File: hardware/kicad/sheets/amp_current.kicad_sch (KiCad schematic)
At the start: 22 parts, among them J11 AMP OUT (+ / -), J12 CRYOCOOLER (+ / -), U17 ISO7741DW, U18 ACS37800KMACTR-030B3-SPI

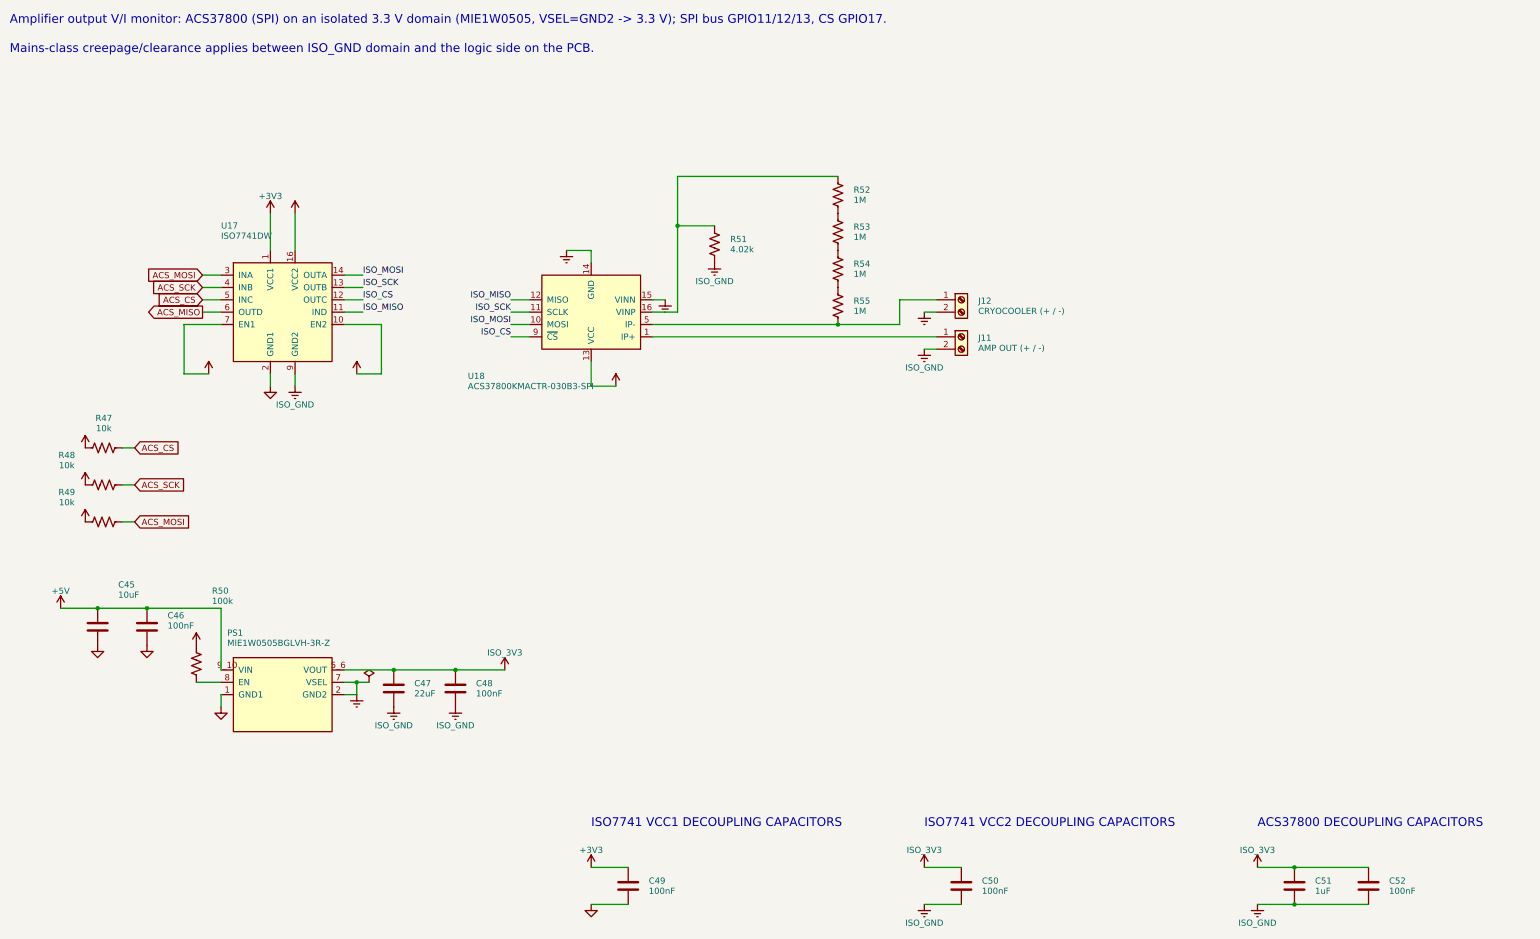
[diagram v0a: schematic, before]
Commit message: Put supply pins on top and grounds on the bottom of IC symbols; flake8-clean Python
Schematic: re-laid out pins on U2, U3, U6, U7, U11, U14, U17-U20, U22-U24
and PS1 (supply on top, ground/strap pins on the bottom edge) via custom
`cryocooler:` symbols (make_lib.from_stock) and a gnd_bus helper; U18/U2
use mirroring instead of a 180 degree rotation. Nets are unchanged (ERC 0,
117/117 datasheet rules, PCB nets still match). Text placement now shows
every power-symbol name, avoids wires, and uses a realistic character width.

Python: black -l 79 -S plus manual wrapping so hardware/kicad and scripts/
pass flake8; add .flake8.

Co-Authored-By: Claude Sonnet 5.5 <noreply@anthropic.com>
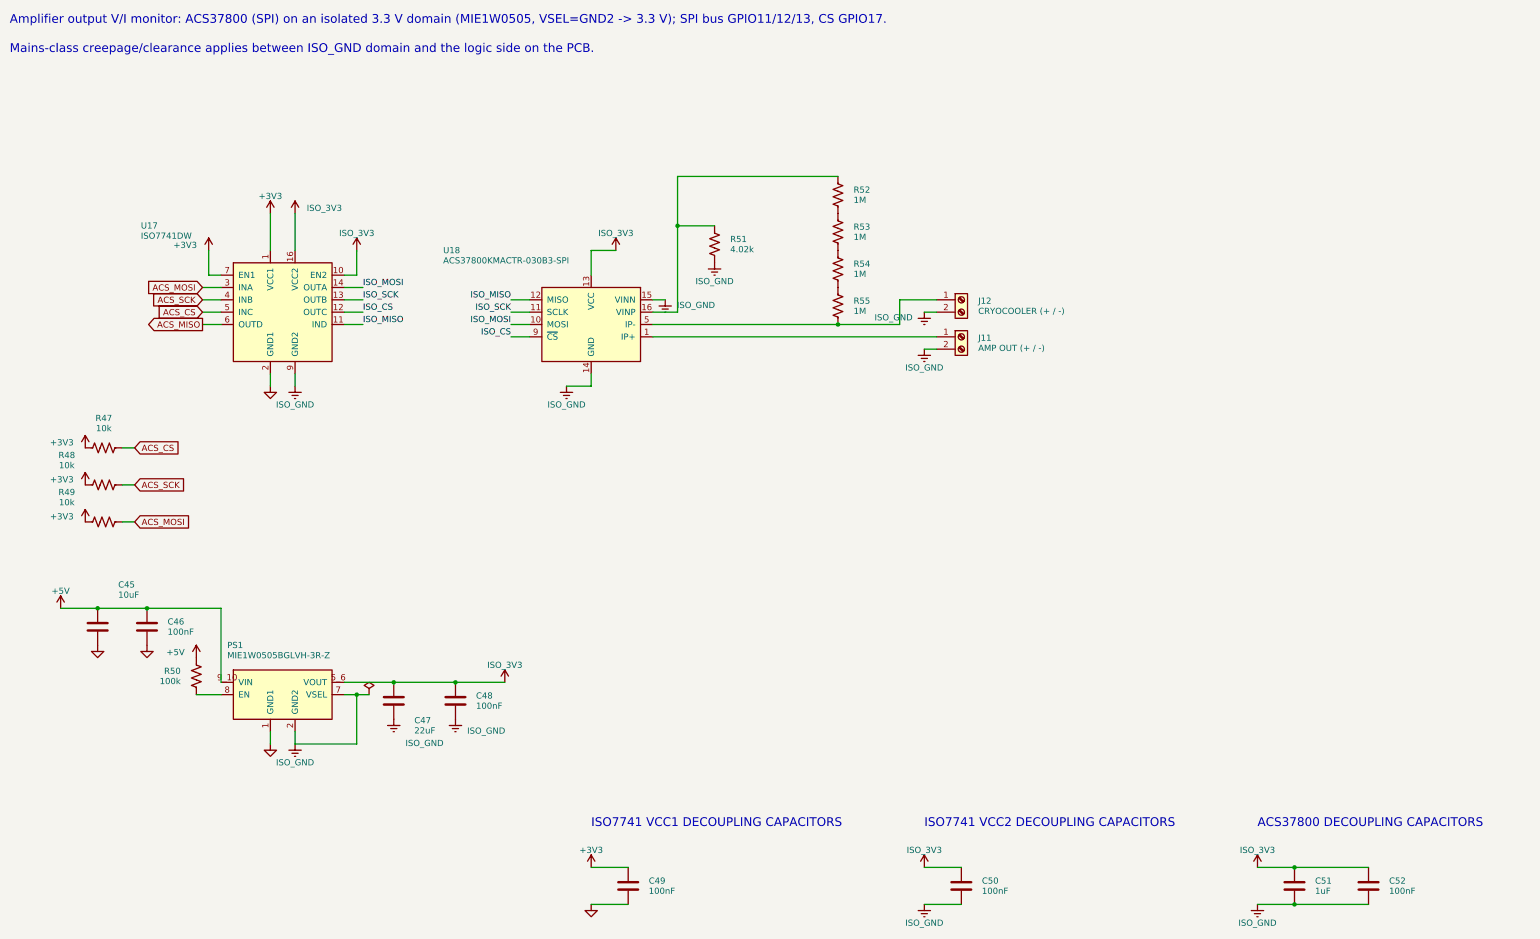
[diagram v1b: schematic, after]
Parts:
- removed C45: 10uF, Capacitor_SMD:C_0805_2012Metric, symbol Device:C
- removed C51: 1uF, Capacitor_SMD:C_0805_2012Metric, symbol Device:C
- removed J11: AMP OUT (+ / -), TerminalBlock_Phoenix:TerminalBlock_Phoenix_MKDS-1,5-2-5.08_1x02_P5.08mm_Horizontal, symbol Connector:Screw_Terminal_01x02
- removed J12: CRYOCOOLER (+ / -), TerminalBlock_Phoenix:TerminalBlock_Phoenix_MKDS-1,5-2-5.08_1x02_P5.08mm_Horizontal, symbol Connector:Screw_Terminal_01x02
- removed PS1: MIE1W0505BGLVH-3R-Z, cryocooler:CONV_MIE1W0505BGLVH-3R-Z, symbol cryocooler:MIE1W0505BGLVH-3R-Z
- removed R55: 1M, Resistor_SMD:R_1206_3216Metric, symbol Device:R_US
- added C49: 100nF, Capacitor_SMD:C_0603_1608Metric, symbol Device:C
- added R48, R49: 10k, Resistor_SMD:R_0603_1608Metric, symbol Device:R_US
- added R51: 4.02k, Resistor_SMD:R_0603_1608Metric, symbol Device:R_US
- added R52, R54: 1M, Resistor_SMD:R_1206_3216Metric, symbol Device:R_US
- C45: renamed from R49; value 10k -> 10uF; footprint Resistor_SMD:R_0603_1608Metric -> Capacitor_SMD:C_0805_2012Metric; symbol Device:R_US -> Device:C
- C51: renamed from C50; value 100nF -> 1uF; footprint Capacitor_SMD:C_0603_1608Metric -> Capacitor_SMD:C_0805_2012Metric
- J11: renamed from R53; value 1M -> AMP OUT (+ / -); footprint Resistor_SMD:R_1206_3216Metric -> TerminalBlock_Phoenix:TerminalBlock_Phoenix_MKDS-1,5-2-5.08_1x02_P5.08mm_Horizontal; symbol Device:R_US -> Connector:Screw_Terminal_01x02
- J12: renamed from R54; value 1M -> CRYOCOOLER (+ / -); footprint Resistor_SMD:R_1206_3216Metric -> TerminalBlock_Phoenix:TerminalBlock_Phoenix_MKDS-1,5-2-5.08_1x02_P5.08mm_Horizontal; symbol Device:R_US -> Connector:Screw_Terminal_01x02
- PS1: renamed from R48; value 10k -> MIE1W0505BGLVH-3R-Z; footprint Resistor_SMD:R_0603_1608Metric -> cryocooler:CONV_MIE1W0505BGLVH-3R-Z; symbol Device:R_US -> cryocooler:MIE1W0505BGLVH-3R-Z
- R53: renamed from R51; value 4.02k -> 1M; footprint Resistor_SMD:R_0603_1608Metric -> Resistor_SMD:R_1206_3216Metric
- renumbered C49 to C50, R52 to R55
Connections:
- net +3V3: now also C49.1, R48.1, R49.1; no longer C45.1, C50.1, PS1.1
- net +5V: now also C45.1, PS1.9_10 (VIN)
- net ACS_MOSI: now also R49.2; no longer C45.2
- net ACS_SCK: now also R48.2; no longer PS1.2
- net GND: now also C45.2, PS1.1 (GND1), PS1.11_12 (GND1), C49.2; no longer C50.2
- net ISO_3V3: now also C50.1, PS1.5_6 (VOUT)
- net ISO_GND: now also C50.2, J11.2 (Pin_2), J12.2 (Pin_2), PS1.2 (GND2), PS1.3_4 (GND2), PS1.7 (VSEL), R51.2; no longer R53.2
- net at R55.2: now also J12.1 (Pin_1), U18.5 (IP-), U18.6 (IP-), U18.7 (IP-), U18.8 (IP-); no longer J11.1
- net at R50.2: now also PS1.8 (EN)
- net at U18.1 (IP+), U18.2 (IP+), U18.3 (IP+)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: now also J11.1 (Pin_1)
- new net: R54.2, R55.1
- new net: R51.1, R52.1, U18.16 (VINP)
- new net: R52.2, R53.1
- new net: R53.2, R54.1
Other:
- moved on the sheet: C50, C51, R53, R55

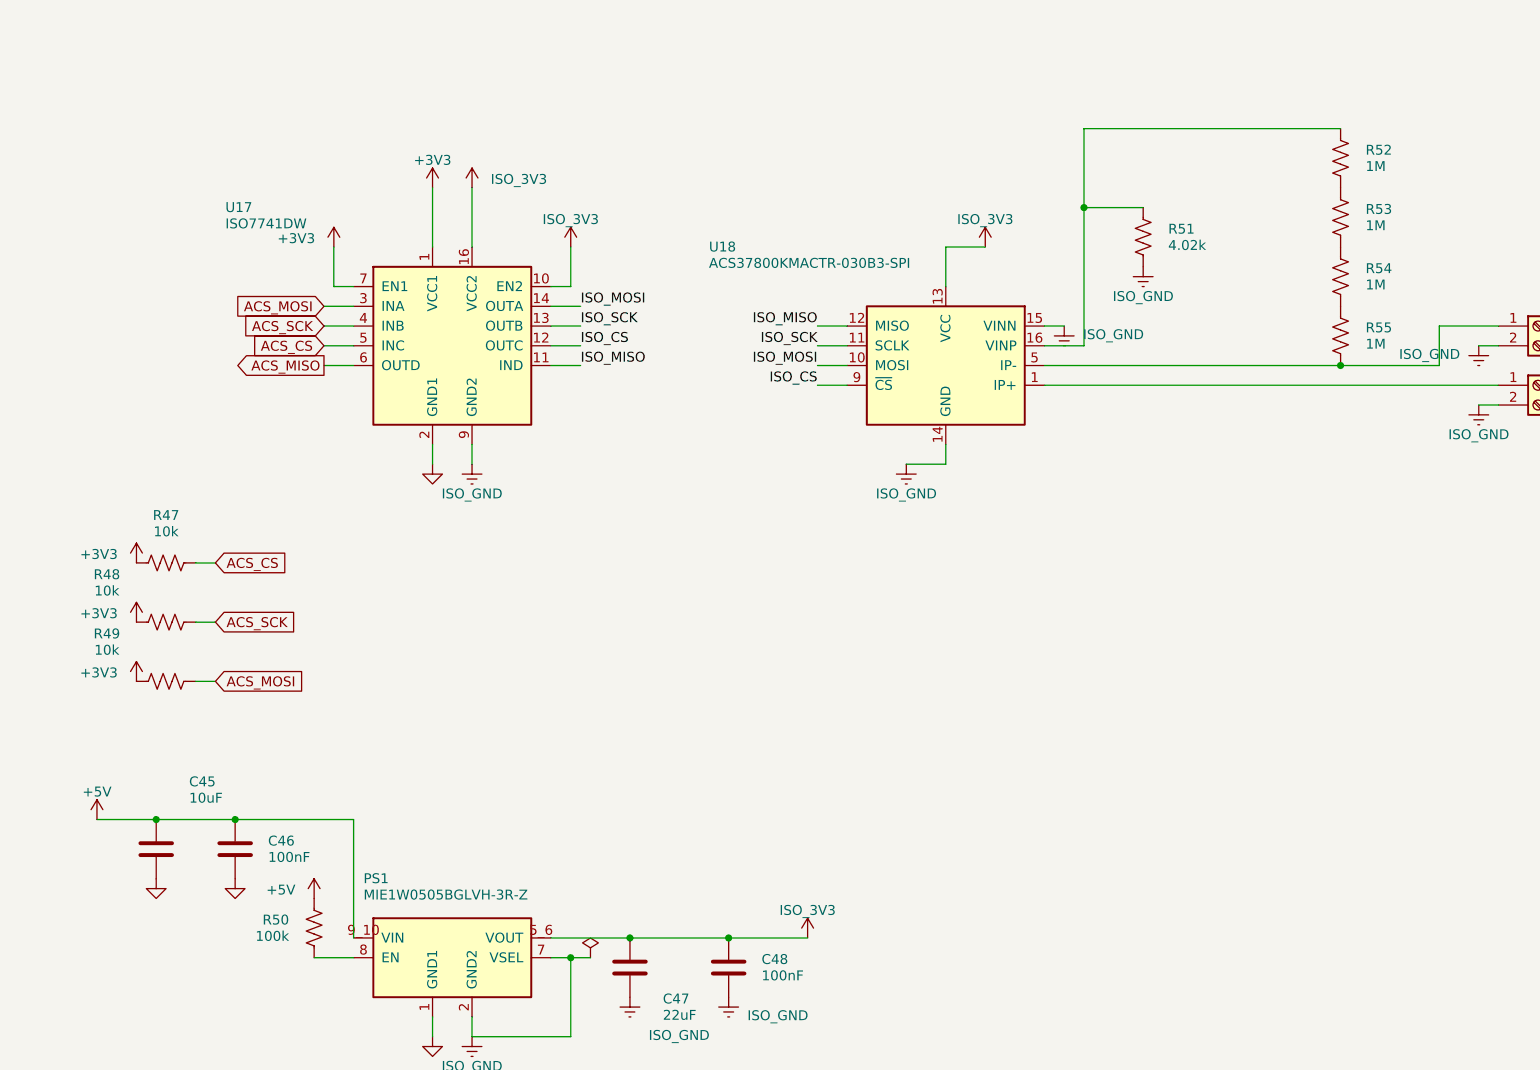
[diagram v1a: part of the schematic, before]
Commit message: KiCad schematic: INA239, ADS1220, SC18IS604 bridge, relay driver, test points
- system_current: INA237 -> INA239 (SPI, CS GPIO3) with the 49.9 ohm / 470 nF
  input filter, power LED and ALERT LED; VBUS shares the filtered IN- node.
- cold_head: ADS122C04 -> ADS1220 (SPI, CS GPIO44).
- i2c_bridge (new): SC18IS604 SPI-to-I2C bridge for the EMC2303, with a
  74LVC1G125 gating its MISO onto the shared bus.
- compressor_relay (new): GPIO16 high-side switch sharing one generator
  function with the amplifier REM switch.
- debug (new): about 40 test points and rail LEDs (the isolated rail LED
  returns to ISO_GND).
- ISO7741 -> ACS37800 SPI lines are straight wires (pins reordered on the
  symbol); USB_VBUS is one wire plus a naming label.
- Custom symbols for INA239, ADS1220, SC18IS604; datasheet rules 117 -> 162;
  GPIO map checks updated. ERC 0.

Co-Authored-By: Claude Sonnet 5.5 <noreply@anthropic.com>
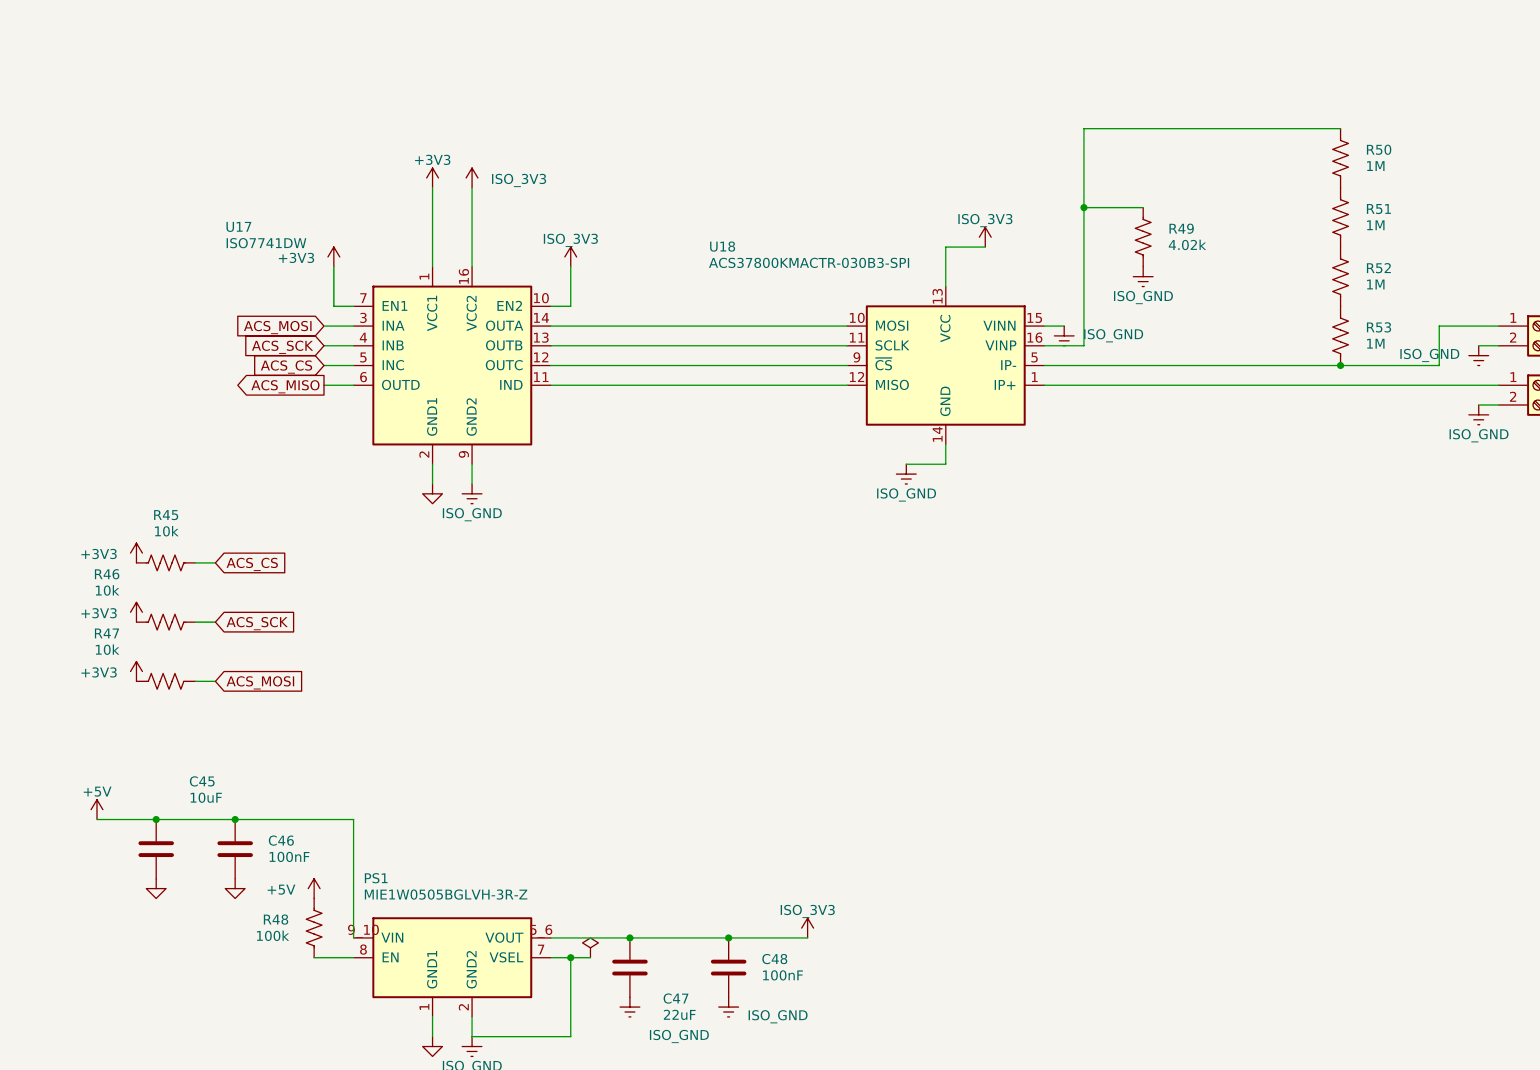
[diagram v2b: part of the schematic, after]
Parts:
- removed C45: 10uF, Capacitor_SMD:C_0805_2012Metric, symbol Device:C
- removed C51: 1uF, Capacitor_SMD:C_0805_2012Metric, symbol Device:C
- removed J11: AMP OUT (+ / -), TerminalBlock_Phoenix:TerminalBlock_Phoenix_MKDS-1,5-2-5.08_1x02_P5.08mm_Horizontal, symbol Connector:Screw_Terminal_01x02
- removed J12: CRYOCOOLER (+ / -), TerminalBlock_Phoenix:TerminalBlock_Phoenix_MKDS-1,5-2-5.08_1x02_P5.08mm_Horizontal, symbol Connector:Screw_Terminal_01x02
- removed PS1: MIE1W0505BGLVH-3R-Z, cryocooler:CONV_MIE1W0505BGLVH-3R-Z, symbol cryocooler:MIE1W0505BGLVH-3R-Z
- removed R55: 1M, Resistor_SMD:R_1206_3216Metric, symbol Device:R_US
- added C49: 100nF, Capacitor_SMD:C_0603_1608Metric, symbol Device:C
- added R45, R46: 10k, Resistor_SMD:R_0603_1608Metric, symbol Device:R_US
- added R48: 100k, Resistor_SMD:R_0603_1608Metric, symbol Device:R_US
- added R49: 4.02k, Resistor_SMD:R_0603_1608Metric, symbol Device:R_US
- added R52: 1M, Resistor_SMD:R_1206_3216Metric, symbol Device:R_US
- C45: renamed from R49; value 10k -> 10uF; footprint Resistor_SMD:R_0603_1608Metric -> Capacitor_SMD:C_0805_2012Metric; symbol Device:R_US -> Device:C
- C51: renamed from C50; value 100nF -> 1uF; footprint Capacitor_SMD:C_0603_1608Metric -> Capacitor_SMD:C_0805_2012Metric
- J11: renamed from R53; value 1M -> AMP OUT (+ / -); footprint Resistor_SMD:R_1206_3216Metric -> TerminalBlock_Phoenix:TerminalBlock_Phoenix_MKDS-1,5-2-5.08_1x02_P5.08mm_Horizontal; symbol Device:R_US -> Connector:Screw_Terminal_01x02
- J12: renamed from R54; value 1M -> CRYOCOOLER (+ / -); footprint Resistor_SMD:R_1206_3216Metric -> TerminalBlock_Phoenix:TerminalBlock_Phoenix_MKDS-1,5-2-5.08_1x02_P5.08mm_Horizontal; symbol Device:R_US -> Connector:Screw_Terminal_01x02
- PS1: renamed from R48; value 10k -> MIE1W0505BGLVH-3R-Z; footprint Resistor_SMD:R_0603_1608Metric -> cryocooler:CONV_MIE1W0505BGLVH-3R-Z; symbol Device:R_US -> cryocooler:MIE1W0505BGLVH-3R-Z
- R50: value 100k -> 1M; footprint Resistor_SMD:R_0603_1608Metric -> Resistor_SMD:R_1206_3216Metric
- R51: value 4.02k -> 1M; footprint Resistor_SMD:R_0603_1608Metric -> Resistor_SMD:R_1206_3216Metric
- renumbered C49 to C50, R52 to R53
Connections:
- net +3V3: now also C49.1, R45.1, R46.1; no longer C45.1, C50.1, PS1.1
- net +5V: now also C45.1, PS1.9_10 (VIN), R48.1; no longer R50.1
- net ACS_CS: now also R45.2; no longer R47.2
- net ACS_MOSI: now also R47.2; no longer C45.2
- net ACS_SCK: now also R46.2; no longer PS1.2
- net GND: now also C45.2, PS1.1 (GND1), PS1.11_12 (GND1), C49.2; no longer C50.2
- net ISO_3V3: now also C50.1, PS1.5_6 (VOUT)
- net ISO_GND: now also C50.2, J11.2 (Pin_2), J12.2 (Pin_2), PS1.2 (GND2), PS1.3_4 (GND2), PS1.7 (VSEL), R49.2; no longer R51.2
- net at U18.5 (IP-), U18.6 (IP-), U18.7 (IP-)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: now also J12.1 (Pin_1), R53.2
- net at U18.1 (IP+), U18.2 (IP+), U18.3 (IP+)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: now also J11.1 (Pin_1)
- net at R50.2: now also R51.1
- net ISO_CS: no longer names the net of U17.12 (OUTC), U18.9 (~{CS})
- net ISO_MISO: no longer names the net of U17.11 (IND), U18.12 (MISO)
- net ISO_MOSI: no longer names the net of U17.14 (OUTA), U18.10 (MOSI)
- net ISO_SCK: no longer names the net of U17.13 (OUTB), U18.11 (SCLK)
- new net: R49.1, R50.1, U18.16 (VINP)
- new net: PS1.8 (EN), R48.2
- new net: R52.2, R53.1
- new net: R51.2, R52.1
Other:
- moved on the sheet: C50, C51, R51, R53

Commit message: Add per-section supply jumpers, 8-pin IMU header and connector pin labels
- Four 1.27 mm 2-pin jumpers (JP1-JP4), each with a rail-on LED, cut the
  supply of one section for debugging: signal generator +3V3, +-15V
  generator +5V in, isolated amp-current supply +5V in, and a shared
  +3V3 net for the cooling chips (EMC2303, RTD ADC, I2C bridge).
- J14 is now an 8-pin JST XH in the Adafruit LSM6DSOX pad order
  (VIN, GND, SCL, SDA, DO, CS, I1, I2); firmware pin comments updated.
- Pin-function labels beside every connector, "RAILS ±15V" box title.
- Board re-placed and re-routed (130 x 110 mm); DRC 0 errors, 0 unconnected,
  ERC 0, 173 datasheet rules pass. BOM, READMEs, Gerbers and renders
  regenerated; link_usb_vbus.py now adapts to the routed layout.

Co-Authored-By: Claude Sonnet 5.5 <noreply@anthropic.com>
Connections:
- net +5V renamed +5V_ISO
